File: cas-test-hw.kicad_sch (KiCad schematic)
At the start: 3 parts

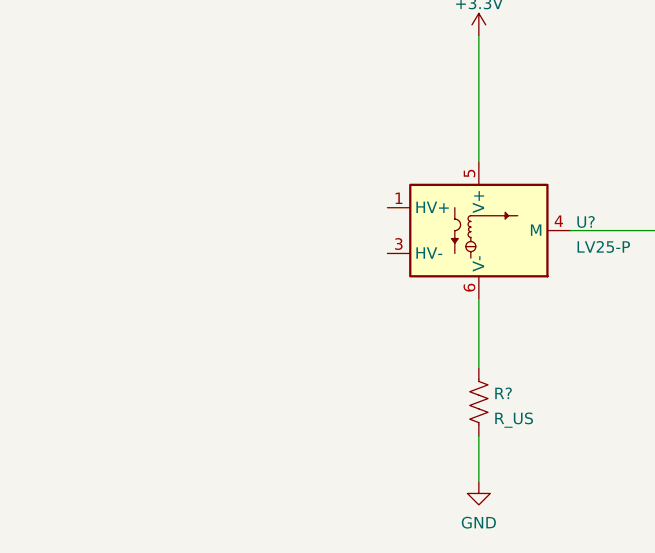
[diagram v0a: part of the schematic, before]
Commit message: added bjt
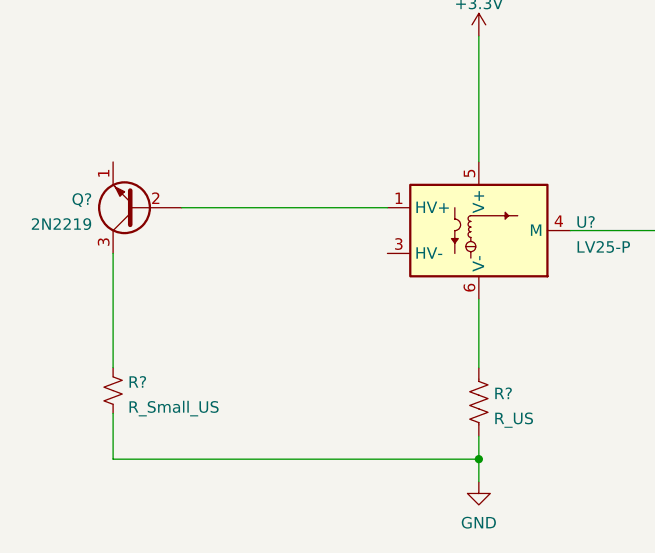
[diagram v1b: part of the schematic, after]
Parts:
- added Q?: 2N2219, Package_TO_SOT_THT:TO-39-3, symbol Transistor_BJT:2N2219
- added R?: R_Small_US, symbol Device:R_Small_US
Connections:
- net GND: now also R?.2
- net at U?.1 (HV+): now also Q?.2 (B)
- new net: Q?.3 (C), R?.1
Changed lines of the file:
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@@
 (kicad_sch (version 20210621) (generator eeschema)
   (paper "A4")
+  (junction (at 123.19 125.73) (diameter 0) (color 0 0 0 0))
+  (wire (pts (xy 82.55 102.87) (xy 82.55 115.57))
+    (stroke (width 0) (type default) (color 0 0 0 0))
+  )
+  (wire (pts (xy 82.55 120.65) (xy 82.55 125.73))
+    (stroke (width 0) (type default) (color 0 0 0 0))
+  )
+  (wire (pts (xy 82.55 125.73) (xy 123.19 125.73))
+    (stroke (width 0) (type default) (color 0 0 0 0))
+  )
+  (wire (pts (xy 90.17 97.79) (xy 113.03 97.79))
+    (stroke (width 0) (type default) (color 0 0 0 0))
+  )
   (wire (pts (xy 123.19 78.74) (xy 123.19 92.71))
     (stroke (width 0) (type default) (color 0 0 0 0))
@@
     (stroke (width 0) (type default) (color 0 0 0 0))
   )
-  (wire (pts (xy 123.19 123.19) (xy 123.19 128.27))
+  (wire (pts (xy 123.19 123.19) (xy 123.19 125.73))
+    (stroke (width 0) (type default) (color 0 0 0 0))
+  )
+  (wire (pts (xy 123.19 125.73) (xy 123.19 128.27))
     (stroke (width 0) (type default) (color 0 0 0 0))
   )
@@
     (pin "1")
   )
+  (symbol (lib_id "Device:R_Small_US") (at 82.55 118.11 0) (unit 1)
+    (in_bom yes) (on_board yes) (fields_autoplaced)
+    (property "Reference" "R?" (id 0) (at 84.201 117.2015 0)
+      (effects (font (size 1.27 1.27)) (justify left))
+    )
+    (property "Value" "R_Small_US" (id 1) (at 84.201 119.9766 0)
+      (effects (font (size 1.27 1.27)) (justify left))
+    )
+    (property "Footprint" "" (id 2) (at 82.55 118.11 0)
+      (effects (font (size 1.27 1.27)) hide)
+    )
+    (property "Datasheet" "~" (id 3) (at 82.55 118.11 0)
+      (effects (font (size 1.27 1.27)) hide)
+    )
+    (pin "1")
+    (pin "2")
+  )
   (symbol (lib_id "Device:R_US") (at 123.19 119.38 0) (unit 1)
     (in_bom yes) (on_board yes) (fields_autoplaced)
@@
     (pin "1")
     (pin "2")
+  )
+  (symbol (lib_id "Transistor_BJT:2N2219") (at 85.09 97.79 180) (unit 1)
+    (in_bom yes) (on_board yes) (fields_autoplaced)
+    (property "Reference" "Q?" (id 0) (at 80.2386 96.8815 0)
+      (effects (font (size 1.27 1.27)) (justify left))
+    )
+    (property "Value" "2N2219" (id 1) (at 80.2386 99.6566 0)
+      (effects (font (size 1.27 1.27)) (justify left))
+    )
+    (property "Footprint" "Package_TO_SOT_THT:TO-39-3" (id 2) (at 80.01 95.885 0)
+      (effects (font (size 1.27 1.27) italic) (justify left) hide)
+    )
+    (property "Datasheet" "http://www.onsemi.com/pub_link/Collateral/2N2219-D.PDF" (id 3) (at 85.09 97.79 0)
+      (effects (font (size 1.27 1.27)) (justify left) hide)
+    )
+    (pin "1")
+    (pin "2")
+    (pin "3")
   )
   (symbol (lib_id "Sensor_Voltage:LV25-P") (at 123.19 100.33 0) (unit 1)
@@
       (reference "#PWR?") (unit 1) (value "GND") (footprint "")
     )
+    (path "/6edfcb88-3354-4cdd-be92-97768716b1e6"
+      (reference "Q?") (unit 1) (value "2N2219") (footprint "Package_TO_SOT_THT:TO-39-3")
+    )
     (path "/25fb7c40-108e-4c3b-a612-05be54d655cb"
       (reference "R?") (unit 1) (value "R_US") (footprint "")
@@
       (reference "R?") (unit 1) (value "R_US") (footprint "")
     )
+    (path "/d933b553-c65a-4939-8aa7-e8a642a50feb"
+      (reference "R?") (unit 1) (value "R_Small_US") (footprint "")
+    )
     (path "/cd7222c6-e829-4e20-bc96-2c7dde7c2e82"

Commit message: new commit from PM
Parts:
- added U?: AD8475xRMZ, Package_SO:MSOP-10_3x3mm_P0.5mm, symbol Amplifier_Difference:AD8475xRMZ
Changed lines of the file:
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@@
     (pin "6")
+  )
+  (symbol (lib_id "Amplifier_Difference:AD8475xRMZ") (at 185.42 45.72 0) (unit 1)
+    (in_bom yes) (on_board yes) (fields_autoplaced)
+    (property "Reference" "U?" (id 0) (at 185.4834 57.9026 0))
+    (property "Value" "AD8475xRMZ" (id 1) (at 185.4834 60.6777 0))
+    (property "Footprint" "Package_SO:MSOP-10_3x3mm_P0.5mm" (id 2) (at 184.15 45.72 0)
+      (effects (font (size 1.27 1.27)) hide)
+    )
+    (property "Datasheet" "https://www.analog.com/media/en/technical-documentation/data-sheets/AD8475.pdf" (id 3) (at 198.12 40.64 0)
+      (effects (font (size 1.27 1.27)) hide)
+    )
+    (pin "1")
+    (pin "10")
+    (pin "2")
+    (pin "3")
+    (pin "4")
+    (pin "5")
+    (pin "6")
+    (pin "7")
+    (pin "8")
+    (pin "9")
   )
   (sheet_instances
@@
       (reference "R?") (unit 1) (value "R_Small_US") (footprint "")
     )
+    (path "/1e0c8dad-35e1-4e81-b01a-c02a50e9fbd2"
+      (reference "U?") (unit 1) (value "AD8475xRMZ") (footprint "Package_SO:MSOP-10_3x3mm_P0.5mm")
+    )
     (path "/cd7222c6-e829-4e20-bc96-2c7dde7c2e82"
